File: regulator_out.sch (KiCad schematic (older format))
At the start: 36 parts

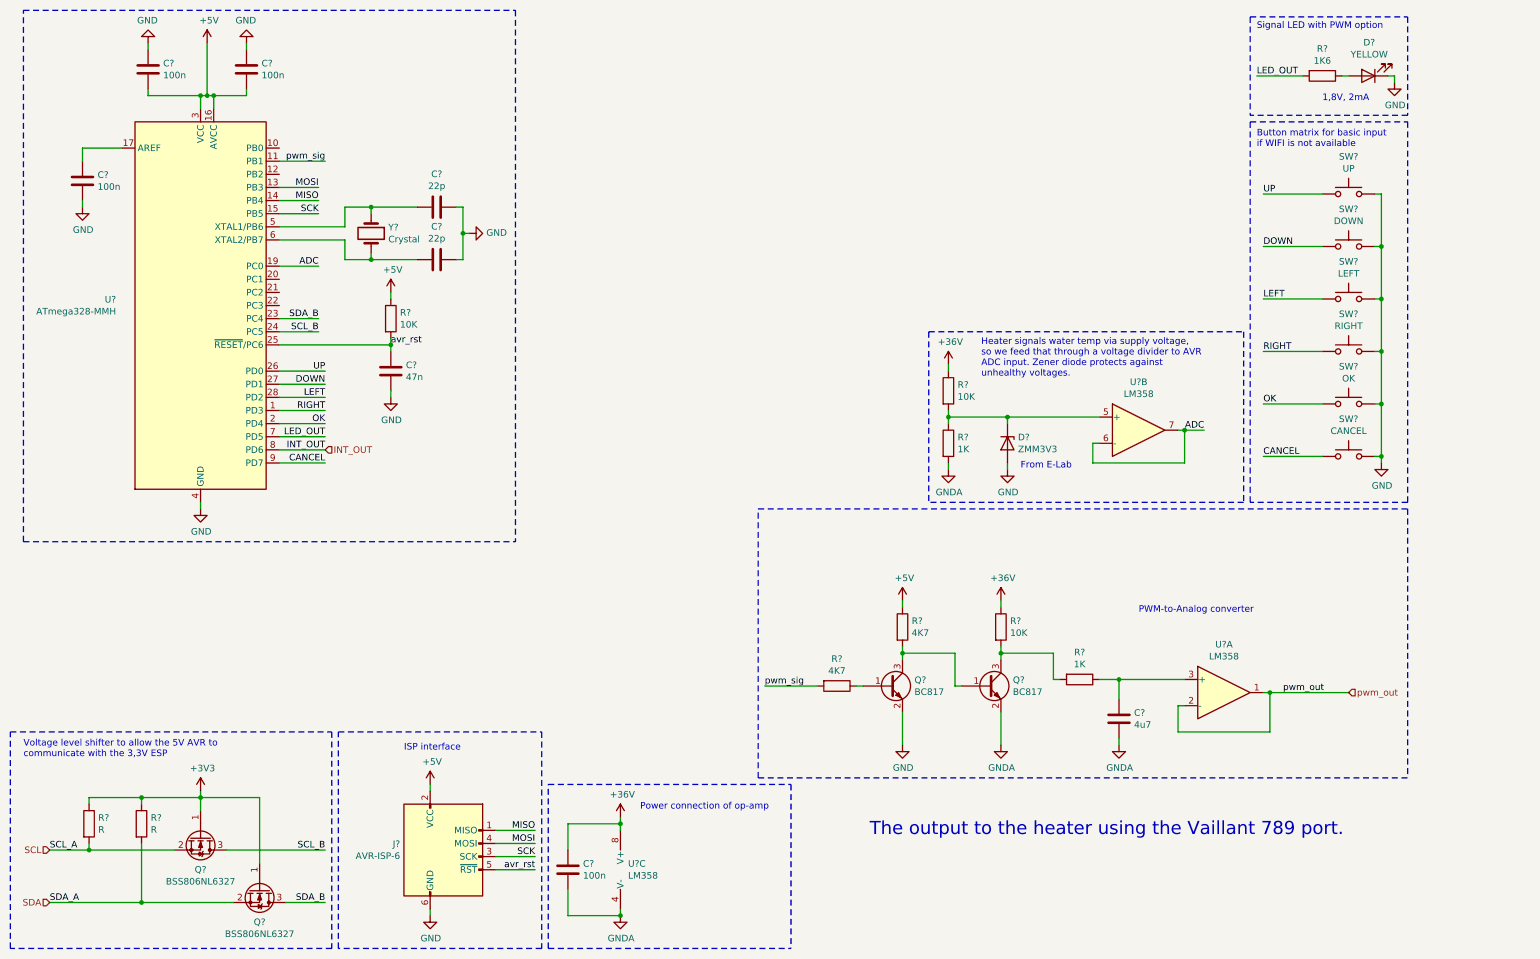
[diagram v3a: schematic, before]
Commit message: Initial draft of thermostat done, beautified circuit diagram.
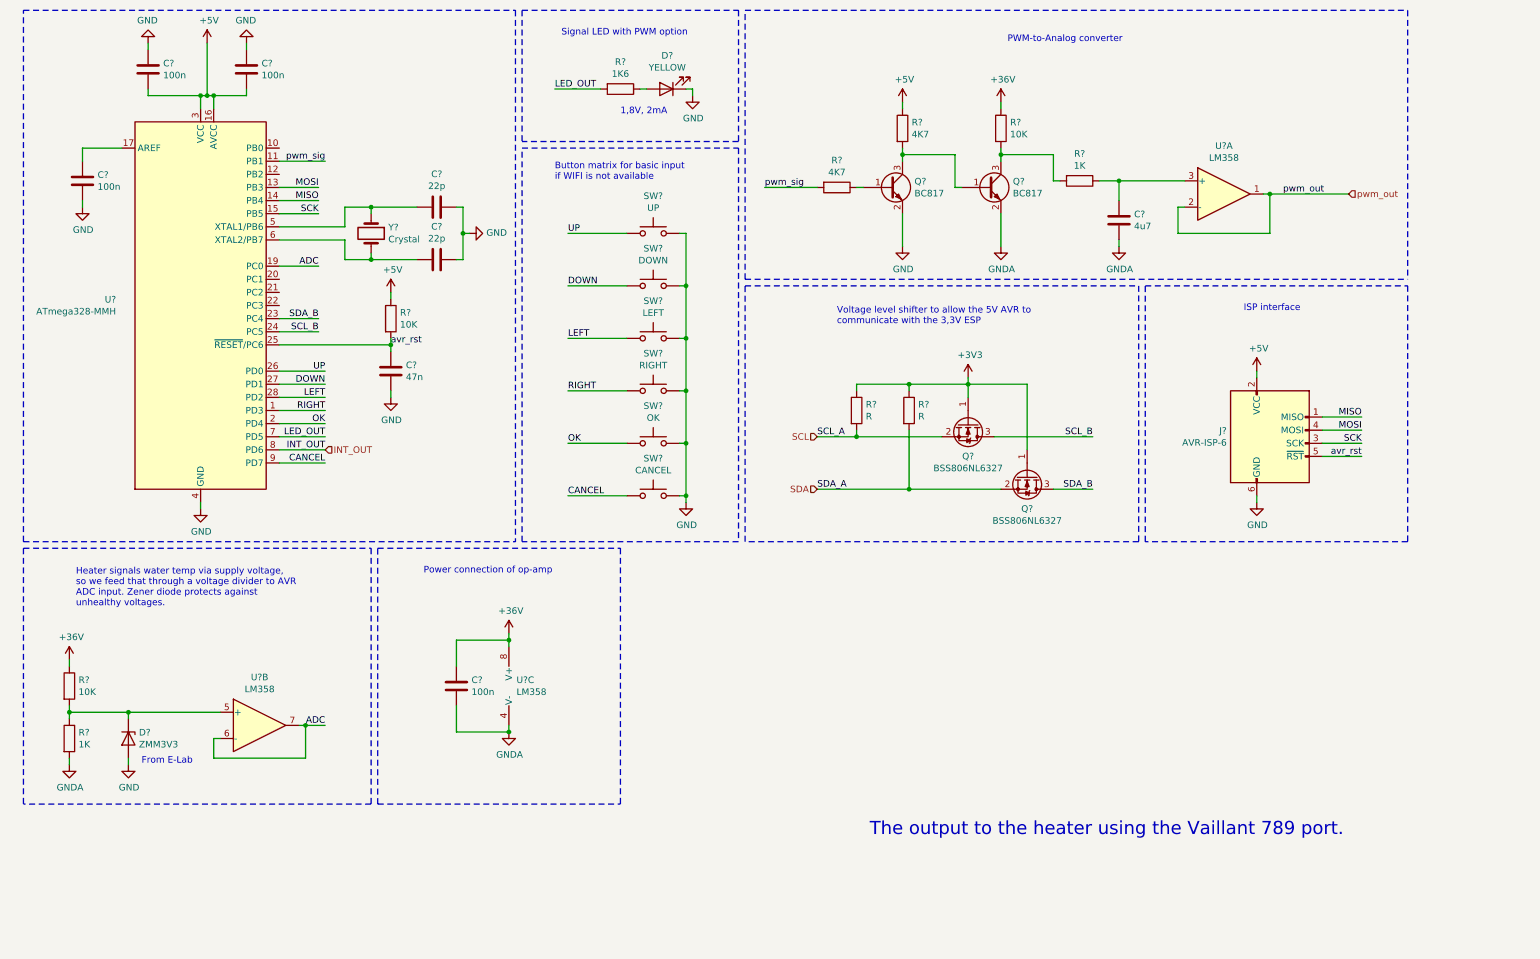
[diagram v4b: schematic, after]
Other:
- moved on the sheet: C?, D?, J?, Q?, R?, SW?, U?A, U?B, U?C

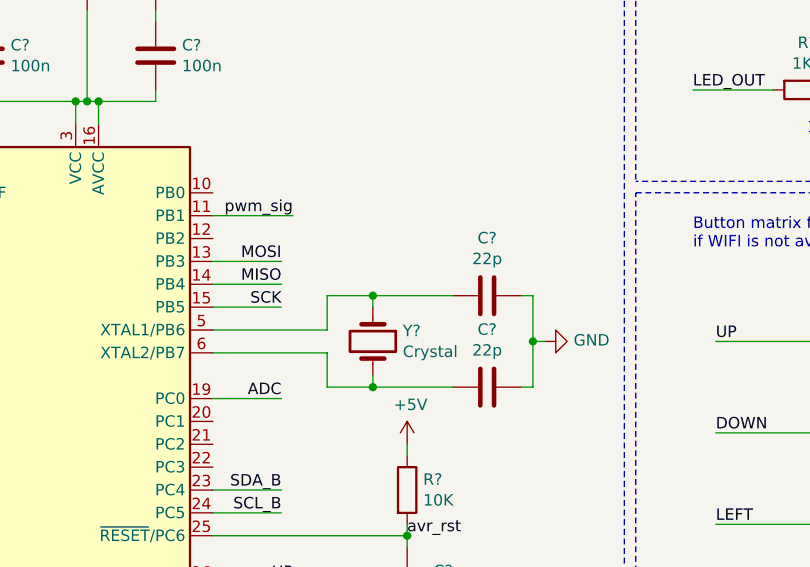
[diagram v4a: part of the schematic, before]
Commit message: Exchanged AVR crystal with one I already have.
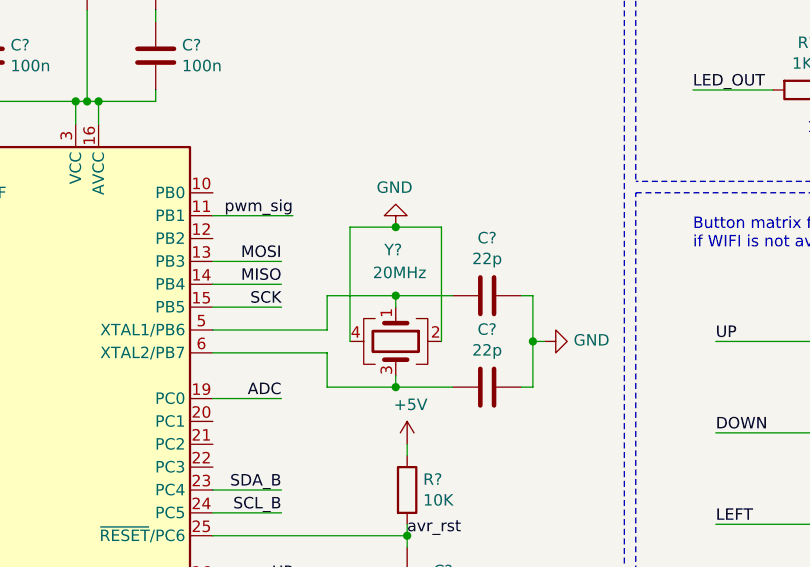
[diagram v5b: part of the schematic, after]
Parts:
- removed Y?: Crystal, symbol Device:Crystal
- added Y?: 20MHz, symbol Device:Crystal_GND24
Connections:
- net GND: now also Y?.2, Y?.4
- net at C?.2, U?.5 (XTAL1/PB6): now also Y?.1
- net at C?.2, U?.6 (XTAL2/PB7): now also Y?.3
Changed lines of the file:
@@
 	3300 6650 5150 6650
-$Comp
-L Device:Crystal Y?
-U 1 1 5E816AB9
-P 3250 2300
-F 0 "Y?" V 3204 2431 50  0000 L CNN
-F 1 "Crystal" V 3295 2431 50  0000 L CNN
-F 2 "" H 3250 2300 50  0001 C CNN
-F 3 "~" H 3250 2300 50  0001 C CNN
-	1    3250 2300
-	0    1    1    0
-$EndComp
 $Comp
 L Device:C C?
@@
 	3050 2250 3050 2100
 Wire Wire Line
-	3050 2100 3250 2100
-Wire Wire Line
-	3250 2150 3250 2100
-Wire Wire Line
 	2550 2350 3050 2350
 Wire Wire Line
 	3050 2350 3050 2500
-Wire Wire Line
-	3050 2500 3250 2500
-Wire Wire Line
-	3250 2450 3250 2500
 Wire Wire Line
 	3900 2100 3950 2100
@@
 Wire Wire Line
 	3950 2300 3950 2500
-Wire Wire Line
-	3600 2100 3250 2100
-Connection ~ 3250 2100
-Wire Wire Line
-	3600 2500 3250 2500
-Connection ~ 3250 2500
 $Comp
 L Switch:SW_Push SW?
@@
 Wire Notes Line
 	600  4650 4350 4650
+$Comp
+L Device:Crystal_GND24 Y?
+U 1 1 5F10F6C0
+P 3350 2300
+F 0 "Y?" V 2950 2250 50  0000 L CNN
+F 1 "20MHz" V 3050 2200 50  0000 L CNN
+F 2 "" H 3350 2300 50  0001 C CNN
+F 3 "~" H 3350 2300 50  0001 C CNN
+	1    3350 2300
+	0    1    1    0
+$EndComp
+Wire Wire Line
+	3050 2100 3350 2100
+Wire Wire Line
+	3050 2500 3350 2500
+Wire Wire Line
+	3350 2450 3350 2500
+Connection ~ 3350 2500
+Wire Wire Line
+	3350 2500 3600 2500
+Wire Wire Line
+	3350 2150 3350 2100
+Connection ~ 3350 2100
+Wire Wire Line
+	3350 2100 3600 2100
+Wire Wire Line
+	3150 2300 3150 1800
+Wire Wire Line
+	3150 1800 3350 1800
+Wire Wire Line
+	3550 1800 3550 2300
+$Comp
+L power:GND #PWR?
+U 1 1 5F13907B
+P 3350 1800
+F 0 "#PWR?" H 3350 1550 50  0001 C CNN
+F 1 "GND" H 3355 1627 50  0000 C CNN
+F 2 "" H 3350 1800 50  0001 C CNN
+F 3 "" H 3350 1800 50  0001 C CNN
+	1    3350 1800
+	-1   0    0    1
+$EndComp
+Connection ~ 3350 1800
+Wire Wire Line
+	3350 1800 3550 1800
 $EndSCHEMATC

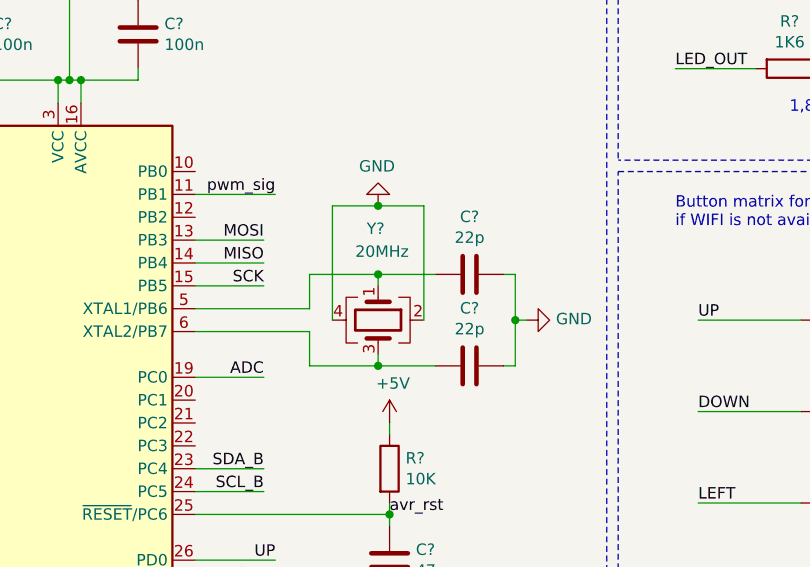
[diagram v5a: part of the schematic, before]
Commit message: Started adding footprints.
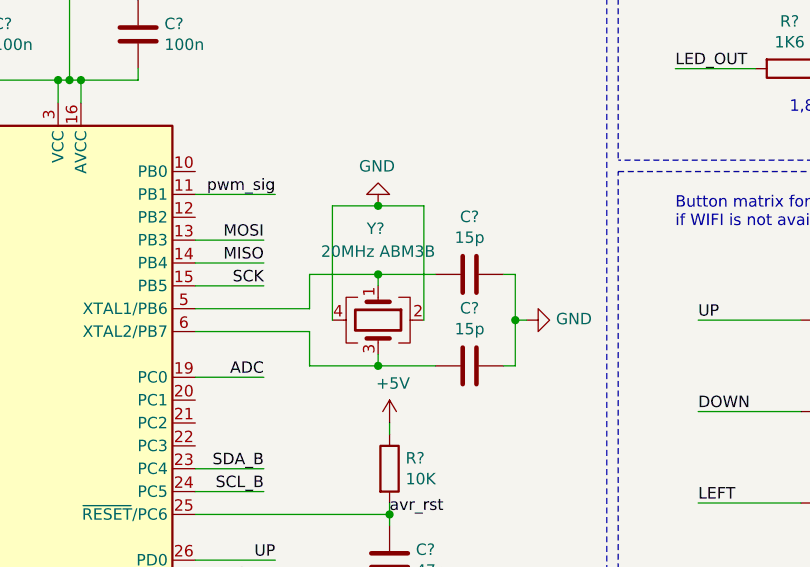
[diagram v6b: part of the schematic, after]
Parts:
- C? (x4): footprint (none) -> Capacitor_SMD:C_0603_1608Metric
- C? (x2): value 22p -> 15p; footprint (none) -> Capacitor_SMD:C_0603_1608Metric
- Y?: value 20MHz -> 20MHz ABM3B; footprint (none) -> Crystal:Crystal_SMD_Abracon_ABM3B-4Pin_5.0x3.2mm
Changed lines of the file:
@@
 $EndComp
 $Comp
-L power:GNDA #PWR?
+L power:GNDA #PWR0145
 U 1 1 5E6E13CC
 P 4300 6100
-F 0 "#PWR?" H 4300 5850 50  0001 C CNN
+F 0 "#PWR0145" H 4300 5850 50  0001 C CNN
 F 1 "GNDA" H 4305 5927 50  0000 C CNN
 F 2 "" H 4300 6100 50  0001 C CNN
@@
 F 0 "C?" H 4015 5796 50  0000 L CNN
 F 1 "100n" H 4015 5705 50  0000 L CNN
-F 2 "" H 3938 5600 50  0001 C CNN
+F 2 "Capacitor_SMD:C_0603_1608Metric" H 3938 5600 50  0001 C CNN
 F 3 "~" H 3900 5750 50  0001 C CNN
 	1    3900 5750
@@
 $EndComp
 $Comp
-L power:+5V #PWR?
+L power:+5V #PWR0146
 U 1 1 5E6EC7FD
 P 2000 850
-F 0 "#PWR?" H 2000 700 50  0001 C CNN
+F 0 "#PWR0146" H 2000 700 50  0001 C CNN
 F 1 "+5V" H 2015 1023 50  0000 C CNN
 F 2 "" H 2000 850 50  0001 C CNN
@@
 F 0 "C?" H 1665 1096 50  0000 L CNN
 F 1 "100n" H 1665 1005 50  0000 L CNN
-F 2 "" H 1588 900 50  0001 C CNN
+F 2 "Capacitor_SMD:C_0603_1608Metric" H 1588 900 50  0001 C CNN
 F 3 "~" H 1550 1050 50  0001 C CNN
 	1    1550 1050
@@
 F 0 "C?" H 2415 1096 50  0000 L CNN
 F 1 "100n" H 2415 1005 50  0000 L CNN
-F 2 "" H 2338 900 50  0001 C CNN
+F 2 "Capacitor_SMD:C_0603_1608Metric" H 2338 900 50  0001 C CNN
 F 3 "~" H 2300 1050 50  0001 C CNN
 	1    2300 1050
@@
 	2050 1250 2300 1250
 $Comp
-L power:GND #PWR?
+L power:GND #PWR0147
 U 1 1 5E6EFBFC
 P 2300 850
-F 0 "#PWR?" H 2300 600 50  0001 C CNN
+F 0 "#PWR0147" H 2300 600 50  0001 C CNN
 F 1 "GND" H 2305 677 50  0000 C CNN
 F 2 "" H 2300 850 50  0001 C CNN
@@
 $EndComp
 $Comp
-L power:GND #PWR?
+L power:GND #PWR0148
 U 1 1 5E6F0102
 P 1550 850
-F 0 "#PWR?" H 1550 600 50  0001 C CNN
+F 0 "#PWR0148" H 1550 600 50  0001 C CNN
 F 1 "GND" H 1555 677 50  0000 C CNN
 F 2 "" H 1550 850 50  0001 C CNN
@@
 F 0 "C?" H 1165 1946 50  0000 L CNN
 F 1 "100n" H 1165 1855 50  0000 L CNN
-F 2 "" H 1088 1750 50  0001 C CNN
+F 2 "Capacitor_SMD:C_0603_1608Metric" H 1088 1750 50  0001 C CNN
 F 3 "~" H 1050 1900 50  0001 C CNN
 	1    1050 1900
@@
 $EndComp
 $Comp
-L power:GND #PWR?
+L power:GND #PWR0149
 U 1 1 5E6F45AB
 P 1050 2100
-F 0 "#PWR?" H 1050 1850 50  0001 C CNN
+F 0 "#PWR0149" H 1050 1850 50  0001 C CNN
 F 1 "GND" H 1055 1927 50  0000 C CNN
 F 2 "" H 1050 2100 50  0001 C CNN
@@
 	1050 1650 1350 1650
 $Comp
-L power:GND #PWR?
+L power:GND #PWR0150
 U 1 1 5E6F6949
 P 1950 4400
-F 0 "#PWR?" H 1950 4150 50  0001 C CNN
+F 0 "#PWR0150" H 1950 4150 50  0001 C CNN
 F 1 "GND" H 1955 4227 50  0000 C CNN
 F 2 "" H 1950 4400 50  0001 C CNN
@@
 $EndComp
 $Comp
-L power:+5V #PWR?
+L power:+5V #PWR0151
 U 1 1 5E6F8A03
 P 3400 2750
-F 0 "#PWR?" H 3400 2600 50  0001 C CNN
+F 0 "#PWR0151" H 3400 2600 50  0001 C CNN
 F 1 "+5V" H 3415 2923 50  0000 C CNN
 F 2 "" H 3400 2750 50  0001 C CNN
@@
 	3400 3100 3400 3150
 $Comp
-L power:GND #PWR?
+L power:GND #PWR0152
 U 1 1 5E6FB219
 P 3400 3550
-F 0 "#PWR?" H 3400 3300 50  0001 C CNN
+F 0 "#PWR0152" H 3400 3300 50  0001 C CNN
 F 1 "GND" H 3405 3377 50  0000 C CNN
 F 2 "" H 3400 3550 50  0001 C CNN
@@
 	10800 4000 10500 4000
 $Comp
-L power:+5V #PWR?
+L power:+5V #PWR0153
 U 1 1 5E70C3C0
 P 10000 3350
-F 0 "#PWR?" H 10000 3200 50  0001 C CNN
+F 0 "#PWR0153" H 10000 3200 50  0001 C CNN
 F 1 "+5V" H 10015 3523 50  0000 C CNN
 F 2 "" H 10000 3350 50  0001 C CNN
@@
 	10000 3350 10000 3400
 $Comp
-L power:GND #PWR?
+L power:GND #PWR0154
 U 1 1 5E70E58C
 P 10000 4350
-F 0 "#PWR?" H 10000 4100 50  0001 C CNN
+F 0 "#PWR0154" H 10000 4100 50  0001 C CNN
 F 1 "GND" H 10005 4177 50  0000 C CNN
 F 2 "" H 10000 4350 50  0001 C CNN
@@
 $EndComp
 $Comp
-L power:+3V3 #PWR?
+L power:+3V3 #PWR0155
 U 1 1 5E715DC3
 P 7800 3400
-F 0 "#PWR?" H 7800 3250 50  0001 C CNN
+F 0 "#PWR0155" H 7800 3250 50  0001 C CNN
 F 1 "+3V3" H 7815 3573 50  0000 C CNN
 F 2 "" H 7800 3400 50  0001 C CNN
@@
 pwm_out
 $Comp
-L power:GNDA #PWR?
+L power:GNDA #PWR0156
 U 1 1 5E6D416A
 P 8950 2400
-F 0 "#PWR?" H 8950 2150 50  0001 C CNN
+F 0 "#PWR0156" H 8950 2150 50  0001 C CNN
 F 1 "GNDA" H 8955 2227 50  0000 C CNN
 F 2 "" H 8950 2400 50  0001 C CNN
@@
 	7300 1300 7300 1350
 $Comp
-L power:+5V #PWR?
+L power:+5V #PWR0157
 U 1 1 5E6D86F0
 P 7300 1300
-F 0 "#PWR?" H 7300 1150 50  0001 C CNN
+F 0 "#PWR0157" H 7300 1150 50  0001 C CNN
 F 1 "+5V" H 7315 1473 50  0000 C CNN
 F 2 "" H 7300 1300 50  0001 C CNN
@@
 	6950 1950 7000 1950
 $Comp
-L power:GND #PWR?
+L power:GND #PWR0158
 U 1 1 5E6D3024
 P 7300 2400
-F 0 "#PWR?" H 7300 2150 50  0001 C CNN
+F 0 "#PWR0158" H 7300 2150 50  0001 C CNN
 F 1 "GND" H 7305 2227 50  0000 C CNN
 F 2 "" H 7300 2400 50  0001 C CNN
@@
 	7300 1700 7300 1750
 $Comp
-L power:GNDA #PWR?
+L power:GNDA #PWR0159
 U 1 1 5E7DE66A
 P 8050 2400
-F 0 "#PWR?" H 8050 2150 50  0001 C CNN
+F 0 "#PWR0159" H 8050 2150 50  0001 C CNN
 F 1 "GNDA" H 8055 2227 50  0000 C CNN
 F 2 "" H 8050 2400 50  0001 C CNN
@@
 	8050 1700 8050 1750
 $Comp
-L power:+36V #PWR?
+L power:+36V #PWR0160
 U 1 1 5E7E489A
 P 8050 1300
-F 0 "#PWR?" H 8050 1150 50  0001 C CNN
+F 0 "#PWR0160" H 8050 1150 50  0001 C CNN
 F 1 "+36V" H 8065 1473 50  0000 C CNN
 F 2 "" H 8050 1300 50  0001 C CNN
@@
 	6100 2650 11150 2650
 $Comp
-L power:+36V #PWR?
+L power:+36V #PWR0161
 U 1 1 5E7E9758
 P 4300 5350
-F 0 "#PWR?" H 4300 5200 50  0001 C CNN
+F 0 "#PWR0161" H 4300 5200 50  0001 C CNN
 F 1 "+36V" H 4315 5523 50  0000 C CNN
 F 2 "" H 4300 5350 50  0001 C CNN
@@
 P 3750 2500
 F 0 "C?" V 3498 2500 50  0000 C CNN
-F 1 "22p" V 3589 2500 50  0000 C CNN
-F 2 "" H 3788 2350 50  0001 C CNN
+F 1 "15p" V 3589 2500 50  0000 C CNN
+F 2 "Capacitor_SMD:C_0603_1608Metric" H 3788 2350 50  0001 C CNN
 F 3 "~" H 3750 2500 50  0001 C CNN
 	1    3750 2500
@@
 P 3750 2100
 F 0 "C?" V 3498 2100 50  0000 C CNN
-F 1 "22p" V 3589 2100 50  0000 C CNN
-F 2 "" H 3788 1950 50  0001 C CNN
+F 1 "15p" V 3589 2100 50  0000 C CNN
+F 2 "Capacitor_SMD:C_0603_1608Metric" H 3788 1950 50  0001 C CNN
 F 3 "~" H 3750 2100 50  0001 C CNN
 	1    3750 2100
@@
 	3950 2500 3900 2500
 $Comp
-L power:GND #PWR?
+L power:GND #PWR0162
 U 1 1 5E8257CF
 P 4000 2300
-F 0 "#PWR?" H 4000 2050 50  0001 C CNN
+F 0 "#PWR0162" H 4000 2050 50  0001 C CNN
 F 1 "GND" V 4005 2172 50  0000 R CNN
 F 2 "" H 4000 2300 50  0001 C CNN
@@
 $EndComp
 $Comp
-L power:GND #PWR?
+L power:GND #PWR0163
 U 1 1 5E83C24C
 P 5650 4350
-F 0 "#PWR?" H 5650 4100 50  0001 C CNN
+F 0 "#PWR0163" H 5650 4100 50  0001 C CNN
 F 1 "GND" H 5655 4177 50  0000 C CNN
 F 2 "" H 5650 4350 50  0001 C CNN
@@
 $EndComp
 $Comp
-L power:GND #PWR?
+L power:GND #PWR0164
 U 1 1 5E8C3BFC
 P 5700 1250
-F 0 "#PWR?" H 5700 1000 50  0001 C CNN
+F 0 "#PWR0164" H 5700 1000 50  0001 C CNN
 F 1 "GND" H 5705 1077 50  0000 C CNN
 F 2 "" H 5700 1250 50  0001 C CNN
@@
 P 950 6350
 AR Path="/5E8EF655" Ref="#PWR?"  Part="1"
-AR Path="/5E6A63AE/5E8EF655" Ref="#PWR?"  Part="1"
-F 0 "#PWR?" H 950 6100 50  0001 C CNN
+AR Path="/5E6A63AE/5E8EF655" Ref="#PWR0165"  Part="1"
+F 0 "#PWR0165" H 950 6100 50  0001 C CNN
 F 1 "GNDA" H 955 6177 50  0000 C CNN
 F 2 "" H 950 6350 50  0001 C CNN
@@
 P 1400 6350
 AR Path="/5E8EF65B" Ref="#PWR?"  Part="1"
-AR Path="/5E6A63AE/5E8EF65B" Ref="#PWR?"  Part="1"
-F 0 "#PWR?" H 1400 6100 50  0001 C CNN
+AR Path="/5E6A63AE/5E8EF65B" Ref="#PWR0166"  Part="1"
+F 0 "#PWR0166" H 1400 6100 50  0001 C CNN
 F 1 "GND" H 1405 6177 50  0000 C CNN
 F 2 "" H 1400 6350 50  0001 C CNN
@@
 P 950 5550
 AR Path="/5E8EF661" Ref="#PWR?"  Part="1"
-AR Path="/5E6A63AE/5E8EF661" Ref="#PWR?"  Part="1"
-F 0 "#PWR?" H 950 5400 50  0001 C CNN
+AR Path="/5E6A63AE/5E8EF661" Ref="#PWR0167"  Part="1"
+F 0 "#PWR0167" H 950 5400 50  0001 C CNN
 F 1 "+36V" H 965 5723 50  0000 C CNN
 F 2 "" H 950 5550 50  0001 C CNN
@@
 P 3350 2300
 F 0 "Y?" V 2950 2250 50  0000 L CNN
-F 1 "20MHz" V 3050 2200 50  0000 L CNN
-F 2 "" H 3350 2300 50  0001 C CNN
+F 1 "20MHz ABM3B" V 3050 2050 50  0000 L CNN
+F 2 "Crystal:Crystal_SMD_Abracon_ABM3B-4Pin_5.0x3.2mm" H 3350 2300 50  0001 C CNN
 F 3 "~" H 3350 2300 50  0001 C CNN
 	1    3350 2300
@@
 	3550 1800 3550 2300
 $Comp
-L power:GND #PWR?
+L power:GND #PWR0168
 U 1 1 5F13907B
 P 3350 1800
-F 0 "#PWR?" H 3350 1550 50  0001 C CNN
+F 0 "#PWR0168" H 3350 1550 50  0001 C CNN
 F 1 "GND" H 3355 1627 50  0000 C CNN
 F 2 "" H 3350 1800 50  0001 C CNN
